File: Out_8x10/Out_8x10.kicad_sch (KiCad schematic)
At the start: 68 parts, among them J1 Conn_01x06, J2 nmount SW Debug, J3 USB_C_Receptacle_USB2.0, J4 Conn_01x06, SW1 Reset, SW2 Boot, SW3 ADDRESS, U1 ADM3483, U2 W25Q128JVSIQ, U3 RP2040, U4 SN74AHCT1G125, U5 AP2112K-3.3, Y1 12MHz,18pF

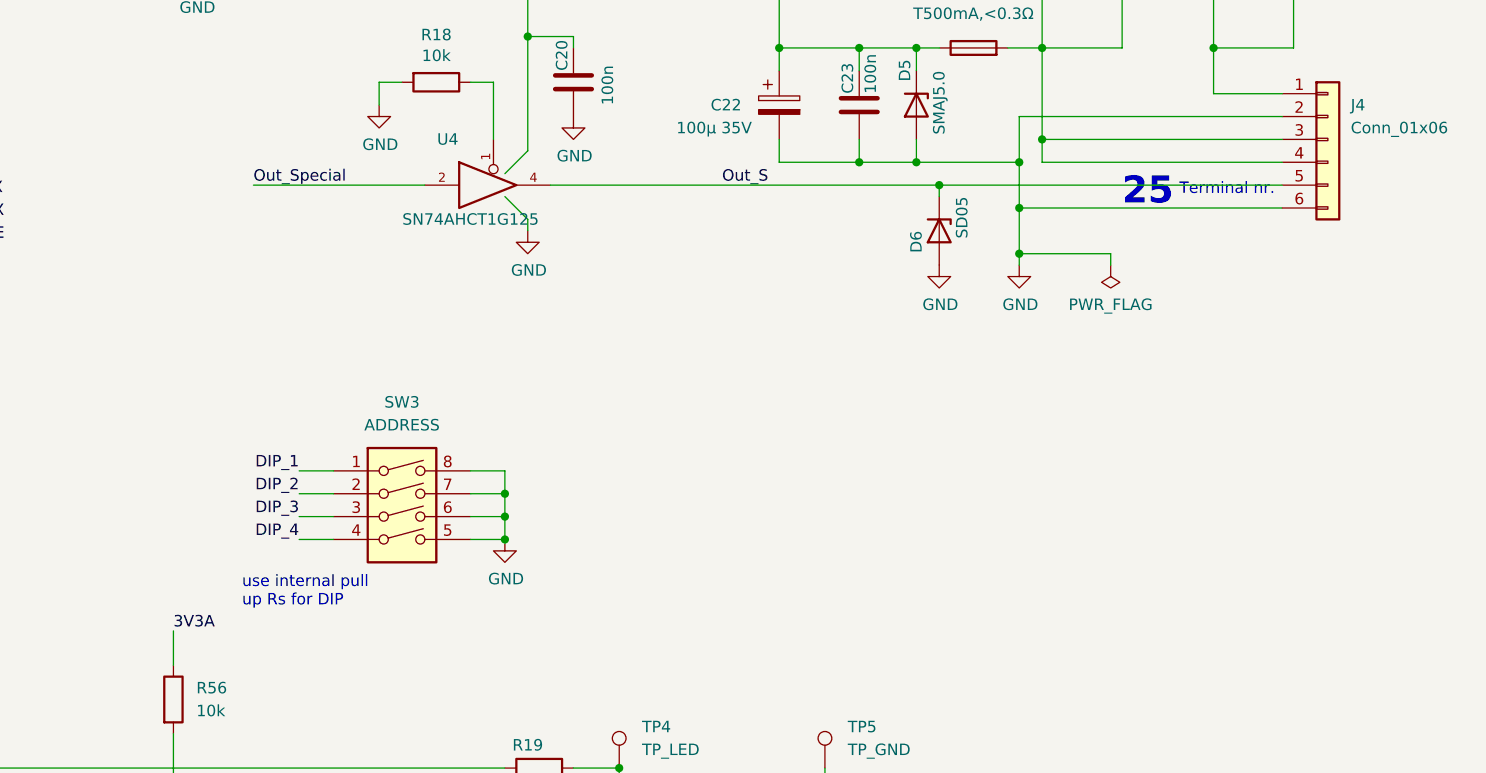
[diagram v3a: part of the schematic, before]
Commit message: updated layout
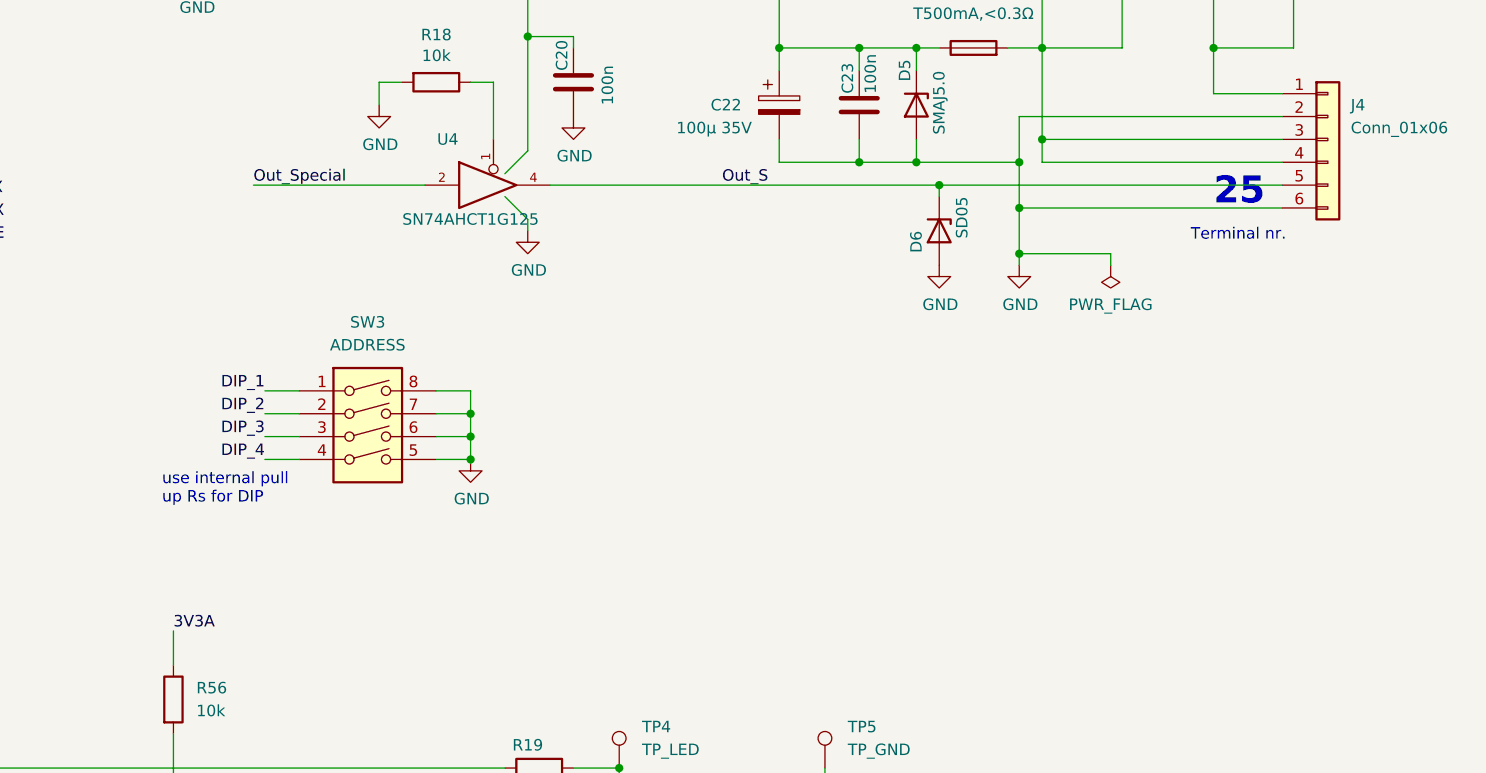
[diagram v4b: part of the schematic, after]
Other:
- moved on the sheet: SW3
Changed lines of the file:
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@@
   (junction (at 100.33 119.38) (diameter 0) (color 0 0 0 0)
   )
-  (junction (at 293.37 134.62) (diameter 0) (color 0 0 0 0)
+  (junction (at 289.56 125.73) (diameter 0) (color 0 0 0 0)
   )
   (junction (at 123.19 60.96) (diameter 0) (color 0 0 0 0)
@@
   (junction (at 109.22 63.5) (diameter 0) (color 0 0 0 0)
   )
-  (junction (at 293.37 129.54) (diameter 0) (color 0 0 0 0)
+  (junction (at 289.56 120.65) (diameter 0) (color 0 0 0 0)
   )
   (junction (at 63.5 54.61) (diameter 0) (color 0 0 0 0)
@@
   (junction (at 295.91 78.74) (diameter 0) (color 0 0 0 0)
   )
-  (junction (at 293.37 132.08) (diameter 0) (color 0 0 0 0)
+  (junction (at 289.56 123.19) (diameter 0) (color 0 0 0 0)
   )
   (junction (at 151.13 142.24) (diameter 0) (color 0 0 0 0)
@@
     (stroke (width 0) (type default) (color 0 0 0 0))
   )
-  (wire (pts (xy 293.37 127) (xy 293.37 129.54))
+  (wire (pts (xy 289.56 118.11) (xy 289.56 120.65))
     (stroke (width 0) (type default) (color 0 0 0 0))
   )
@@
     (stroke (width 0) (type default) (color 0 0 0 0))
   )
-  (wire (pts (xy 289.56 134.62) (xy 293.37 134.62))
+  (wire (pts (xy 285.75 125.73) (xy 289.56 125.73))
     (stroke (width 0) (type default) (color 0 0 0 0))
   )
@@
     (stroke (width 0) (type default) (color 0 0 0 0))
   )
-  (wire (pts (xy 289.56 127) (xy 293.37 127))
+  (wire (pts (xy 285.75 118.11) (xy 289.56 118.11))
     (stroke (width 0) (type default) (color 0 0 0 0))
   )
@@
     (stroke (width 0) (type default) (color 0 0 0 0))
   )
-  (wire (pts (xy 270.51 127) (xy 274.32 127))
+  (wire (pts (xy 266.7 118.11) (xy 270.51 118.11))
     (stroke (width 0) (type default) (color 0 0 0 0))
   )
@@
     (stroke (width 0) (type default) (color 0 0 0 0))
   )
-  (wire (pts (xy 293.37 132.08) (xy 293.37 134.62))
+  (wire (pts (xy 289.56 123.19) (xy 289.56 125.73))
     (stroke (width 0) (type default) (color 0 0 0 0))
   )
@@
     (stroke (width 0) (type default) (color 0 0 0 0))
   )
-  (wire (pts (xy 270.51 129.54) (xy 274.32 129.54))
+  (wire (pts (xy 266.7 120.65) (xy 270.51 120.65))
     (stroke (width 0) (type default) (color 0 0 0 0))
   )
@@
     (stroke (width 0) (type default) (color 0 0 0 0))
   )
-  (wire (pts (xy 270.51 134.62) (xy 274.32 134.62))
+  (wire (pts (xy 266.7 125.73) (xy 270.51 125.73))
     (stroke (width 0) (type default) (color 0 0 0 0))
   )
@@
     (stroke (width 0) (type default) (color 0 0 0 0))
   )
-  (wire (pts (xy 289.56 132.08) (xy 293.37 132.08))
+  (wire (pts (xy 285.75 123.19) (xy 289.56 123.19))
     (stroke (width 0) (type default) (color 0 0 0 0))
   )
@@
     (stroke (width 0) (type default) (color 0 0 0 0))
   )
-  (wire (pts (xy 293.37 129.54) (xy 293.37 132.08))
+  (wire (pts (xy 289.56 120.65) (xy 289.56 123.19))
     (stroke (width 0) (type default) (color 0 0 0 0))
   )
@@
     (stroke (width 0) (type default) (color 0 0 0 0))
   )
-  (wire (pts (xy 270.51 132.08) (xy 274.32 132.08))
+  (wire (pts (xy 266.7 123.19) (xy 270.51 123.19))
     (stroke (width 0) (type default) (color 0 0 0 0))
   )
@@
     (stroke (width 0) (type default) (color 0 0 0 0))
   )
-  (wire (pts (xy 289.56 129.54) (xy 293.37 129.54))
+  (wire (pts (xy 285.75 120.65) (xy 289.56 120.65))
     (stroke (width 0) (type default) (color 0 0 0 0))
   )
@@
     (stroke (width 0) (type default) (color 0 0 0 0))
   )
-  (text "use internal pull\nup Rs for DIP" (at 264.16 142.24 0)
+  (text "use internal pull\nup Rs for DIP" (at 255.27 130.81 0)
     (effects (font (size 1.27 1.27)) (justify left bottom))
   )
@@
     (effects (font (size 1.27 1.27)) (justify left bottom))
   )
-  (text "Terminal nr." (at 368.3 96.52 0)
+  (text "Terminal nr." (at 369.57 101.6 0)
     (effects (font (size 1.27 1.27)) (justify left bottom))
   )
@@
     (effects (font (size 1.27 1.27)) (justify left bottom))
   )
-  (text "25" (at 361.95 97.79 0)
+  (text "25" (at 372.11 97.79 0)
     (effects (font (size 3 3) (thickness 0.6) bold) (justify left bottom))
   )
@@
     (effects (font (size 1.27 1.27)) (justify left bottom))
   )
-  (label "DIP_2" (at 270.51 129.54 180)
+  (label "DIP_2" (at 266.7 120.65 180)
     (effects (font (size 1.27 1.27)) (justify right bottom))
   )
@@
     (effects (font (size 1.27 1.27)) (justify left bottom))
   )
-  (label "DIP_1" (at 270.51 127 180)
+  (label "DIP_1" (at 266.7 118.11 180)
     (effects (font (size 1.27 1.27)) (justify right bottom))
   )
@@
     (effects (font (size 1.27 1.27)) (justify left bottom))
   )
-  (label "DIP_3" (at 270.51 132.08 180)
+  (label "DIP_3" (at 266.7 123.19 180)
     (effects (font (size 1.27 1.27)) (justify right bottom))
   )
@@
     (effects (font (size 1.27 1.27)) (justify right bottom))
   )
-  (label "DIP_4" (at 270.51 134.62 180)
+  (label "DIP_4" (at 266.7 125.73 180)
     (effects (font (size 1.27 1.27)) (justify right bottom))
   )
@@
     (pin "2")
   )
-  (symbol (lib_id "Switch:SW_DIP_x04") (at 281.94 132.08 0) (unit 1)
+  (symbol (lib_id "Switch:SW_DIP_x04") (at 278.13 123.19 0) (unit 1)
     (in_bom yes) (on_board yes) (fields_autoplaced)
-    (property "Reference" "SW3" (id 0) (at 281.94 119.38 0))
-    (property "Value" "ADDRESS" (id 1) (at 281.94 121.92 0))
-    (property "Footprint" "Button_Switch_SMD:SW_DIP_SPSTx04_Slide_6.7x11.72mm_W8.61mm_P2.54mm_LowProfile" (id 2) (at 281.94 132.08 0)
-      (effects (font (size 1.27 1.27)) hide)
-    )
-    (property "Datasheet" "~" (id 3) (at 281.94 132.08 0)
+    (property "Reference" "SW3" (id 0) (at 278.13 110.49 0))
+    (property "Value" "ADDRESS" (id 1) (at 278.13 113.03 0))
+    (property "Footprint" "Button_Switch_SMD:SW_DIP_SPSTx04_Slide_6.7x11.72mm_W8.61mm_P2.54mm_LowProfile" (id 2) (at 278.13 123.19 0)
+      (effects (font (size 1.27 1.27)) hide)
+    )
+    (property "Datasheet" "~" (id 3) (at 278.13 123.19 0)
       (effects (font (size 1.27 1.27)) hide)
     )
@@
     (pin "1")
   )
-  (symbol (lib_id "power:GND") (at 293.37 134.62 0) (unit 1)
-    (in_bom yes) (on_board yes)
-    (property "Reference" "#PWR0138" (id 0) (at 293.37 140.97 0)
-      (effects (font (size 1.27 1.27)) hide)
-    )
-    (property "Value" "GND" (id 1) (at 293.497 139.0142 0))
-    (property "Footprint" "" (id 2) (at 293.37 134.62 0)
-      (effects (font (size 1.27 1.27)) hide)
-    )
-    (property "Datasheet" "" (id 3) (at 293.37 134.62 0)
-      (effects (font (size 1.27 1.27)) hide)
-    )
+  (symbol (lib_id "power:GND") (at 289.56 125.73 0) (unit 1)
+    (in_bom yes) (on_board yes)
+    (property "Reference" "#PWR0138" (id 0) (at 289.56 132.08 0)
+      (effects (font (size 1.27 1.27)) hide)
+    )
+    (property "Value" "GND" (id 1) (at 289.687 130.1242 0))
+    (property "Footprint" "" (id 2) (at 289.56 125.73 0)
+      (effects (font (size 1.27 1.27)) hide)
+    )
+    (property "Datasheet" "" (id 3) (at 289.56 125.73 0)
+      (effects (font (size 1.27 1.27)) hide)
+    )

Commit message: Analog DIP
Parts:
- added C42: 100n, Capacitor_SMD:C_0402_1005Metric, symbol Device:C
- added R57, R60, R61, R64: 2k, Resistor_SMD:R_0603_1608Metric, symbol Device:R
- added R58, R62: 1k, Resistor_SMD:R_0402_1005Metric, symbol Device:R
- added R59: 5k, Resistor_SMD:R_0603_1608Metric, symbol Device:R
- added R63: 3k, Resistor_SMD:R_0603_1608Metric, symbol Device:R
- added TP3, TP6, TP7, TP8: TP_IO27, TestPoint:TestPoint_Pad_D1.0mm, symbol Connector:TestPoint
- added U14: LMV321, Package_TO_SOT_SMD:SOT-23-5, symbol Amplifier_Operational:LMV321
- R56: value 10k -> 33k
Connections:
- net 3V3A: now also C42.1, U14.5 (V+)
- net GND: now also C42.2, R57.2, R58.2, U14.2 (V-); no longer SW3.5, SW3.6, SW3.7, SW3.8
- net Lo_1: now also U3.15 (GPIO12); no longer U3.27 (GPIO16)
- net Lo_10: now also U3.5 (GPIO3); no longer U3.9 (GPIO7)
- net Lo_2: now also U3.14 (GPIO11); no longer U3.18 (GPIO15)
- net Lo_3: now also U3.13 (GPIO10); no longer U3.17 (GPIO14)
- net Lo_4: now also U3.12 (GPIO9); no longer U3.16 (GPIO13)
- net Lo_5: now also U3.11 (GPIO8); no longer U3.15 (GPIO12)
- net Lo_6: now also U3.9 (GPIO7); no longer U3.14 (GPIO11)
- net Lo_7: now also U3.8 (GPIO6); no longer U3.13 (GPIO10)
- net Lo_8: now also U3.7 (GPIO5); no longer U3.12 (GPIO9)
- net Lo_9: now also U3.6 (GPIO4); no longer U3.11 (GPIO8)
- net at R56.2: now also R57.1, U14.1 (+); no longer U3.40 (GPIO28_ADC2)
- net DIP_1: no longer names the net of SW3.1
- net DIP_1: now also R58.1, R62.1, U14.3 (-); no longer U3.5 (GPIO3)
- net DIP_2: no longer names the net of SW3.2
- net DIP_2: now also SW3.3, R60.1, R61.1; no longer U3.6 (GPIO4)
- removed net DIP_3: SW3.3, U3.7 (GPIO5)
- net DIP_4 renamed V_addr
- net V_addr: now also U3.40 (GPIO28_ADC2), R59.1, U14.4; no longer U3.8 (GPIO6)
- new net: R61.2, R62.2, SW3.7, SW3.8
- new net: TP6.1, U3.17 (GPIO14)
- new net: TP3.1, U3.16 (GPIO13)
- new net: TP7.1, U3.18 (GPIO15)
- new net: TP8.1, U3.27 (GPIO16)
- new net: R59.2, R63.1
- new net: R63.2, R64.2, SW3.5, SW3.6
- new net: R60.2, R64.1
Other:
- note added: "DIP V_addr 0000 3,024 0001 2,835 0010 2,646 0011 2,457 0100 2,268 0101 2,079 0110 1,89 0111 1,701 1000 1,512 1001 1,323 1010 1,134 1011 0,945 1100 0,756 1101 0,567 1110 0,378 1111 0,189"
- note removed: "use internal pull up Rs for DIP"
- moved on the sheet: TP2
